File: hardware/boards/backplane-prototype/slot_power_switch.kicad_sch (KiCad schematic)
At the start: 57 parts, among them Q1 BSS123, Q10 BSS123, Q11 SQD50P06-15L_GE3, Q12 SQD50P06-15L_GE3, Q2 BSS123, Q3 SQD50P06-15L_GE3, Q4 SQD50P06-15L_GE3, Q5 BSS123, Q6 BSS123, Q7 SQD50P06-15L_GE3, Q8 SQD50P06-15L_GE3, Q9 BSS123, U1 TCA9548APWR, U2 PCA9554PWR

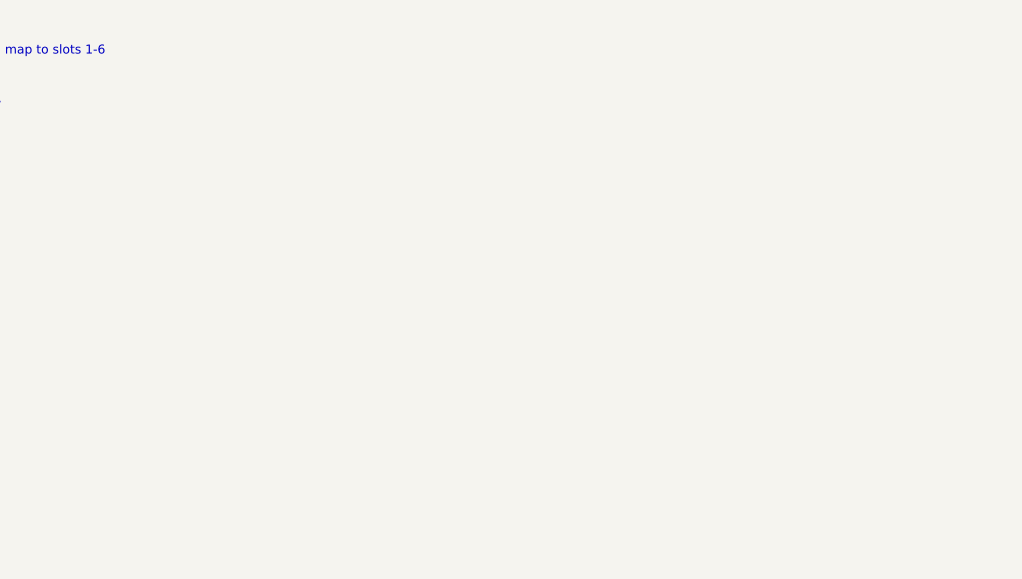
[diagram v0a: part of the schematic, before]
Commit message: hardware: prototype mux address selector
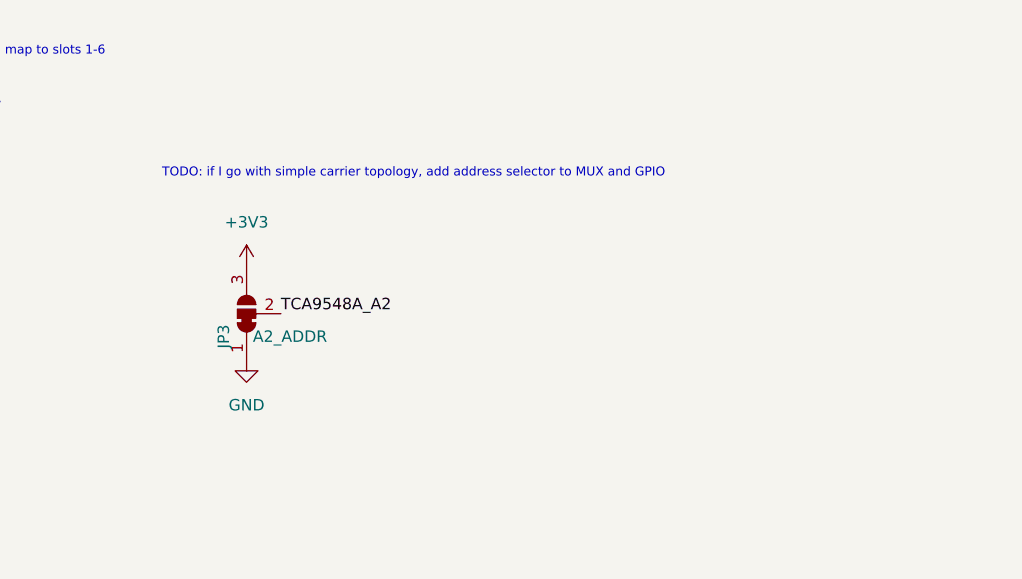
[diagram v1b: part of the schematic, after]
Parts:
- added JP3: A2_ADDR, Jumper:SolderJumper-3_P1.3mm_Bridged12_Pad1.0x1.5mm, symbol Jumper:SolderJumper_3_Bridged12
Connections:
- net +3V3: now also JP3.3 (B)
- net GND: now also JP3.1 (A)
- new net TCA9548A_A2: JP3.2 (C)
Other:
- note added: "TODO: if I go with simple carrier topology, add address selector to MUX and GPIO"
